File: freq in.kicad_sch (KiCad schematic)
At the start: 2 parts, among them IC9 DAC104S085CISDX_NOPB, U5 LM239PT

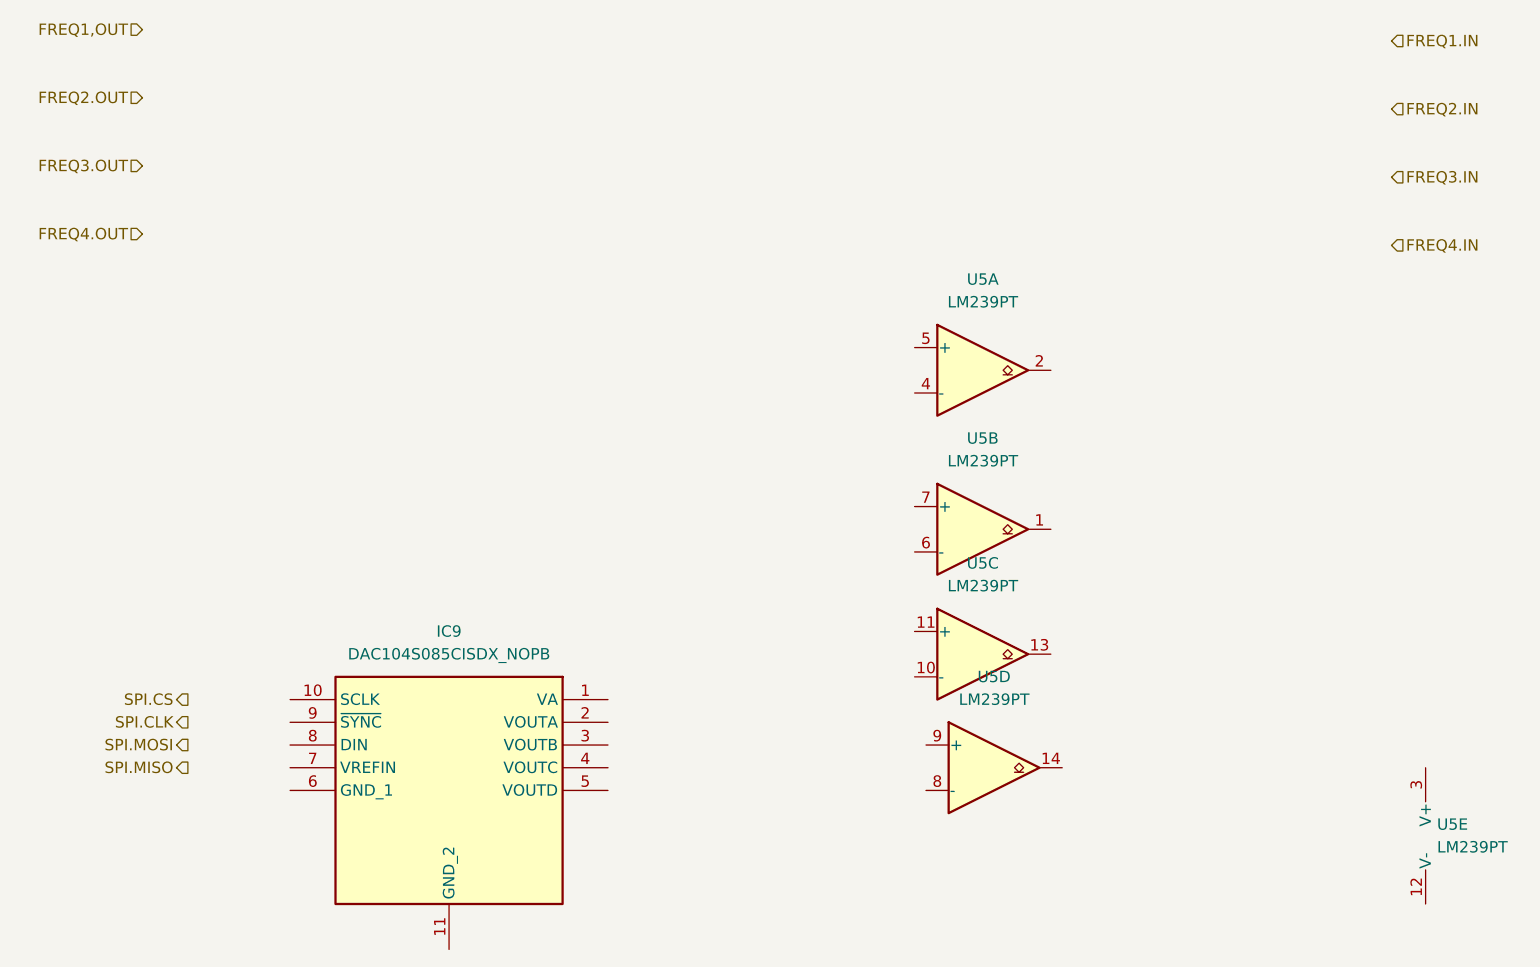
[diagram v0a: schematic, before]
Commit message: Finished schematic of the FreqIn channels
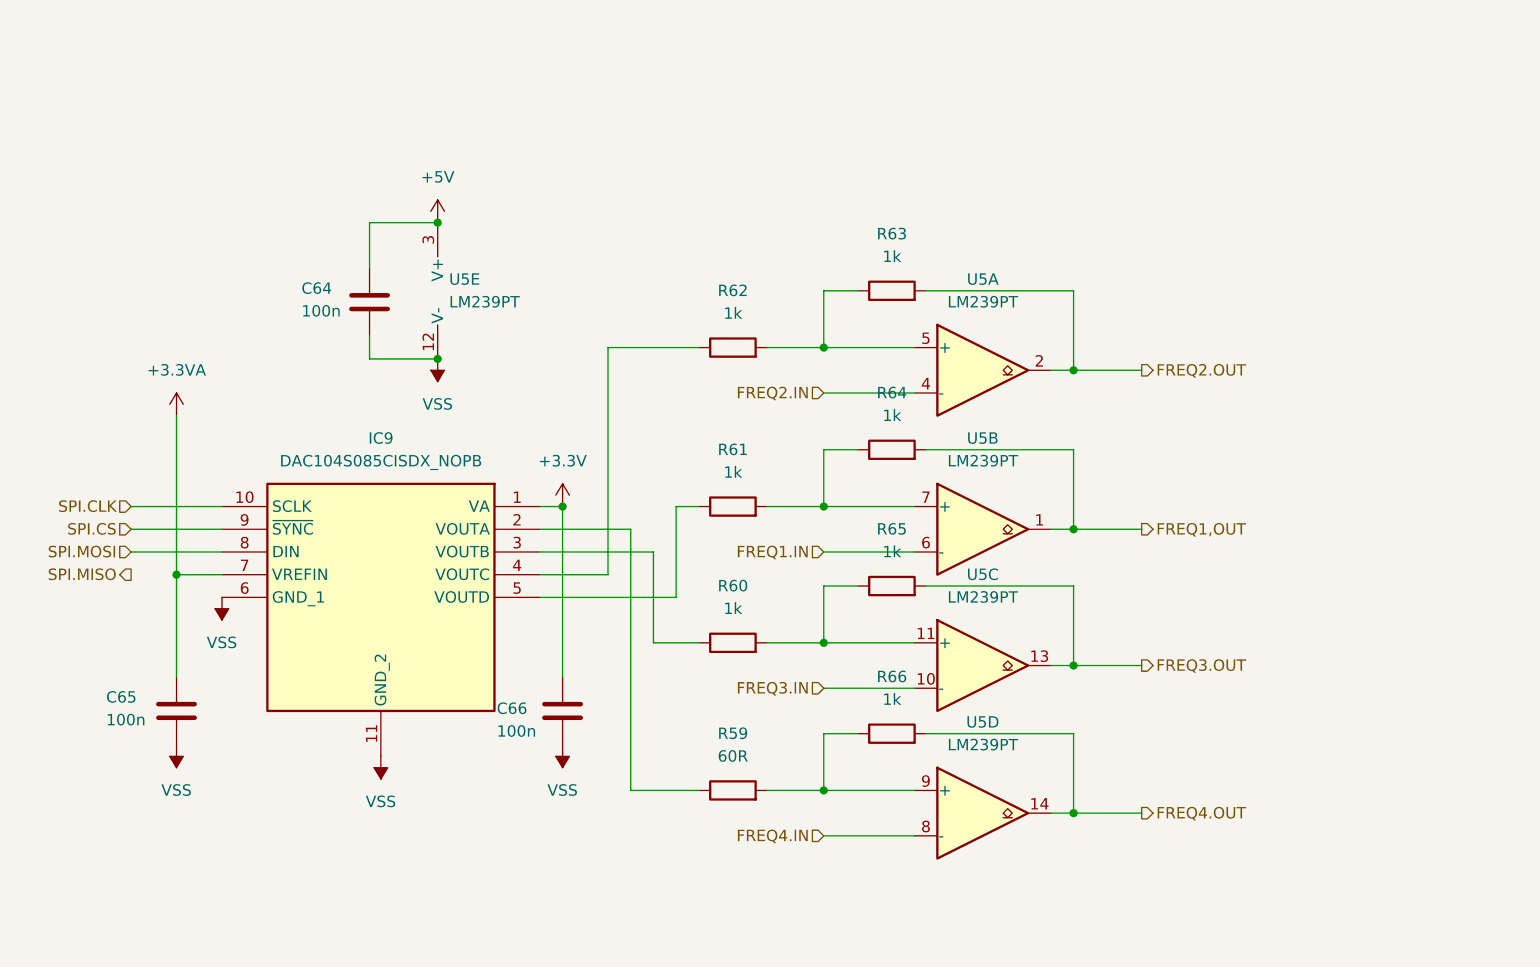
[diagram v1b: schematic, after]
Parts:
- added C64, C65, C66: 100n, Capacitor_SMD:C_0603_1608Metric, symbol Device:C
- added R59: 60R, Resistor_SMD:R_0603_1608Metric, symbol Device:R
- added R60, R61, R62, R63, R64, R65, R66: 1k, Resistor_SMD:R_0603_1608Metric, symbol Device:R
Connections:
- net FREQ1,OUT: now also U5.1, R64.2
- net FREQ1.IN: now also U5.6 (-)
- net FREQ2.IN: now also U5.4 (-)
- net FREQ2.OUT: now also U5.2, R63.2
- net FREQ3.IN: now also U5.10 (-)
- net FREQ3.OUT: now also U5.13, R65.2
- net FREQ4.IN: now also U5.8 (-)
- net FREQ4.OUT: now also U5.14, R66.2
- net SPI.CLK: now also IC9.10 (SCLK)
- net SPI.CS: now also IC9.9 (~{SYNC})
- net SPI.MOSI: now also IC9.8 (DIN)
- net at U5.7 (+): now also R61.2, R64.1
- net +3.3V: now reaches IC9.1 (VA)
- net +3.3V: now also C66.1
- net VSS: now reaches IC9.11 (GND_2)
- net VSS: now also IC9.6 (GND_1), U5.12 (V-), C64.2, C65.2, C66.2
- net at IC9.2 (VOUTA): now also R59.1
- net at IC9.3 (VOUTB): now also R60.1
- net at IC9.4 (VOUTC): now also R62.1
- net at IC9.5 (VOUTD): now also R61.1
- net +3.3VA: now reaches IC9.7 (VREFIN)
- net +3.3VA: now also C65.1
- net at U5.5 (+): now also R62.2, R63.1
- net at U5.9 (+): now also R59.2, R66.1
- net at U5.11 (+): now also R60.2, R65.1
- net +5V: now reaches U5.3 (V+)
- net +5V: now also C64.1
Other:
- moved on the sheet: IC9, U5C, U5D, U5E

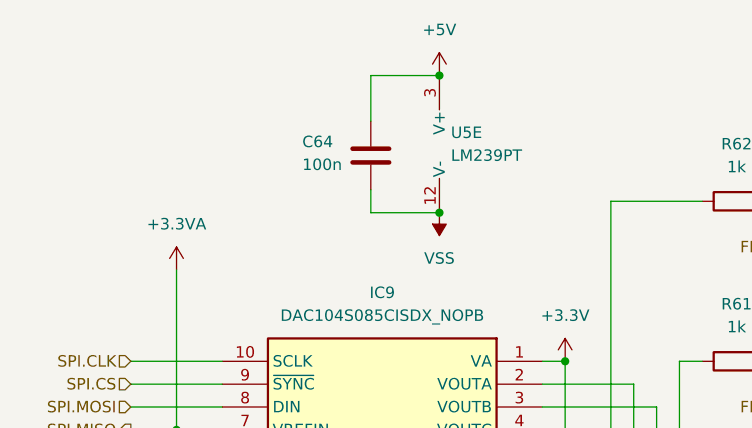
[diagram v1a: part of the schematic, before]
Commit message: Added missing parts of IOcan schematic
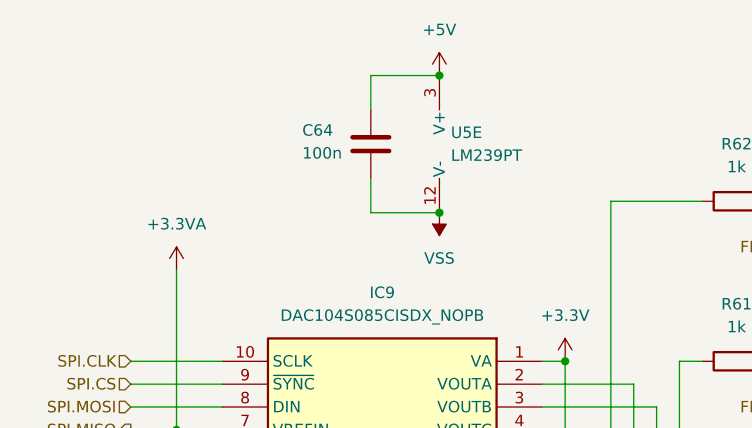
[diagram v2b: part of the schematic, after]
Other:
- moved on the sheet: C64
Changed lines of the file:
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@@
 	(wire
 		(pts
-			(xy 78.74 71.12) (xy 78.74 66.04)
+			(xy 78.74 69.85) (xy 78.74 66.04)
 		)
 		(stroke
@@
 	(wire
 		(pts
-			(xy 78.74 78.74) (xy 78.74 81.28)
+			(xy 78.74 77.47) (xy 78.74 81.28)
 		)
 		(stroke
@@
 	(symbol
 		(lib_id "Device:C")
-		(at 78.74 74.93 0)
+		(at 78.74 73.66 0)
 		(unit 1)
 		(body_style 1)
@@
 		(dnp no)
 		(property "Reference" "C64"
-			(at 71.12 73.406 0)
+			(at 71.12 72.136 0)
 			(show_name no)
 			(do_not_autoplace no)
@@
 		)
 		(property "Value" "100n"
-			(at 71.12 75.946 0)
+			(at 71.12 74.676 0)
 			(show_name no)
 			(do_not_autoplace no)
@@
 		)
 		(property "Footprint" "Capacitor_SMD:C_0603_1608Metric"
-			(at 79.7052 78.74 0)
+			(at 79.7052 77.47 0)
 			(hide yes)
 			(show_name no)
@@
 		)
 		(property "Datasheet" ""
-			(at 78.74 74.93 0)
+			(at 78.74 73.66 0)
 			(hide yes)
 			(show_name no)
@@
 		)
 		(property "Description" "Unpolarized capacitor"
-			(at 78.74 74.93 0)
-			(hide yes)
-			(show_name no)
+			(at 78.74 73.66 0)
+			(hide yes)
+			(show_name no)

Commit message: Checked pinouts
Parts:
- C64, C65, C66: value 100n -> 100n/6.3V
- R63, R64, R65, R66: value 1k -> 220k
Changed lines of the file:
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@@
 			)
 		)
-		(property "Value" "100n"
+		(property "Value" "100n/6.3V"
 			(at 49.276 121.666 0)
 			(show_name no)
@@
 			)
 		)
-		(property "Value" "100n"
+		(property "Value" "100n/6.3V"
 			(at 71.12 74.676 0)
 			(show_name no)
@@
 			)
 		)
-		(property "Value" "1k"
+		(property "Value" "220k"
 			(at 137.16 119.38 90)
 			(show_name no)
@@
 			)
 		)
-		(property "Value" "1k"
+		(property "Value" "220k"
 			(at 137.16 87.63 90)
 			(show_name no)
@@
 			)
 		)
-		(property "Value" "1k"
+		(property "Value" "220k"
 			(at 137.16 69.85 90)
 			(show_name no)
@@
 			)
 		)
-		(property "Value" "1k"
+		(property "Value" "220k"
 			(at 137.16 102.87 90)
 			(show_name no)
@@
 			)
 		)
-		(property "Value" "100n"
+		(property "Value" "100n/6.3V"
 			(at 92.964 122.936 0)
 			(show_name no)
